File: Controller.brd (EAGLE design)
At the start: 100 x 66 mm, 20 parts, among them IC1 TB6612FNG

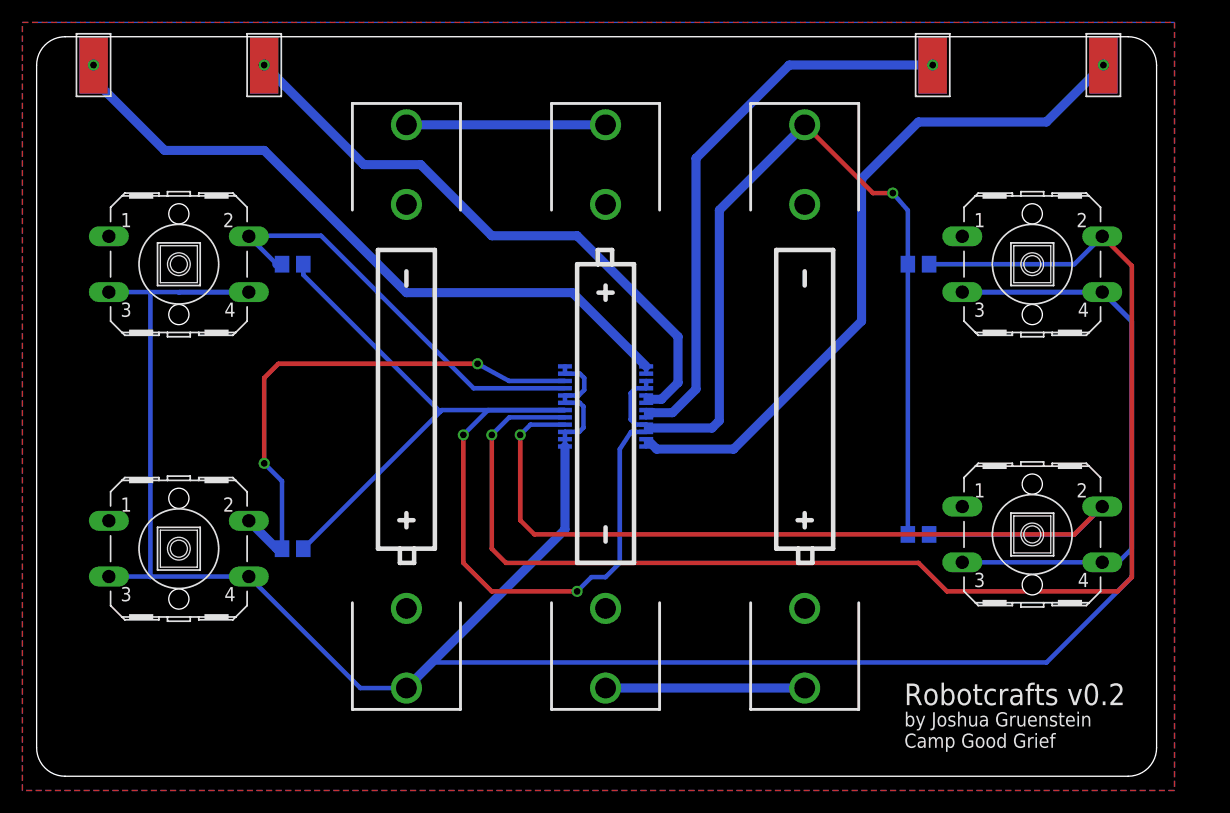
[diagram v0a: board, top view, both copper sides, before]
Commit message: cosmetic PCB upgrades
added OSHW logo to bottom silkscreen
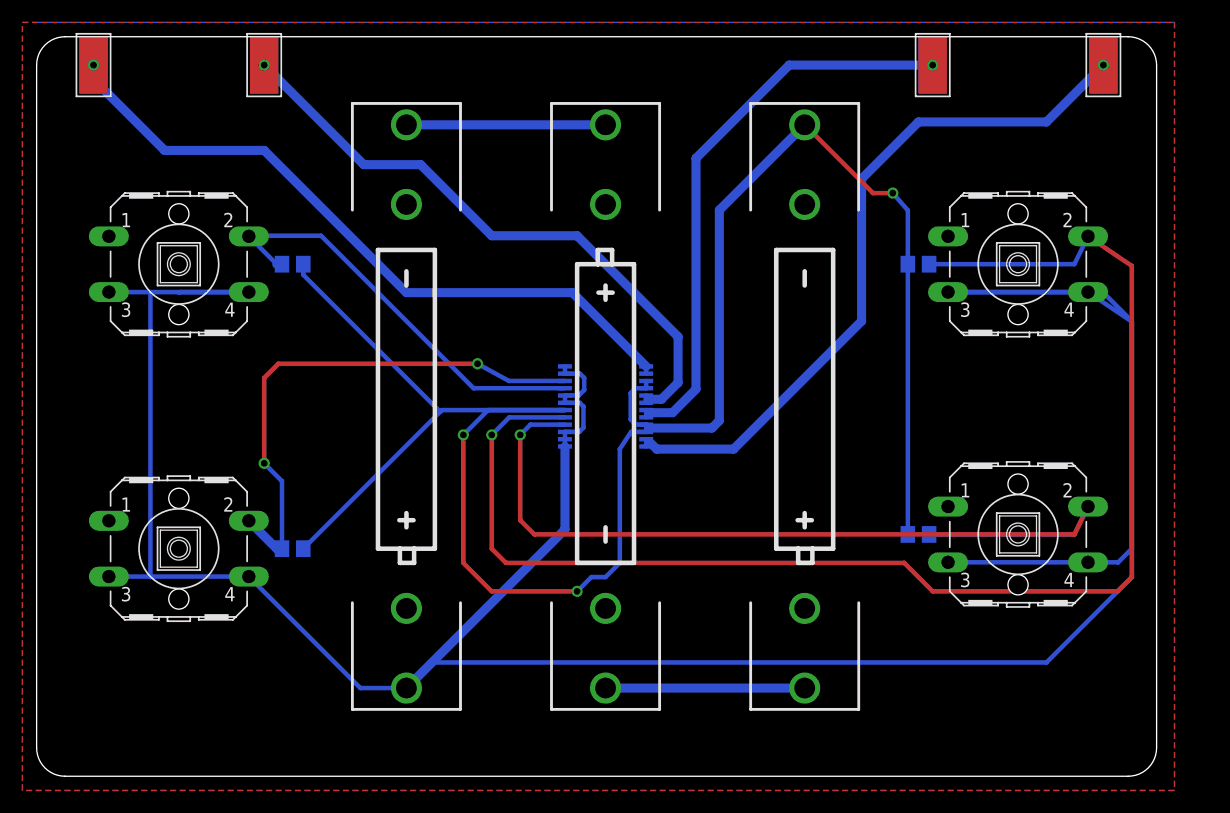
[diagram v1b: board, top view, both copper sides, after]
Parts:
- added GOLD_ORB_SM1: OSHWLOGO_GOLD_ORB_MED, bfl:OSHW1
- moved R_BCK_BTN 1.27 mm to (87.6, 21.6)
- moved R_FWD_BTN 1.27 mm to (87.6, 45.7)
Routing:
- net VCC: track 275.5 -> 279.0 mm
- net R_BCK: track 82.0 -> 80.5 mm
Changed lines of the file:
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@@
 <wire x1="97.46" y1="66.03" x2="2.54" y2="66.03" width="0" layer="20"/>
 <wire x1="2.54" y1="66.03" x2="0" y2="63.49" width="0" layer="20" curve="90"/>
-<text x="77.47" y="6.35" size="1.9304" layer="25">Robotcrafts v0.2</text>
-<text x="77.47" y="2.54" size="1.27" layer="25">by Joshua Gruenstein
+<text x="97.79" y="6.35" size="1.9304" layer="26" rot="MR0">Robotcrafts v0.2</text>
+<text x="97.79" y="2.54" size="1.27" layer="26" rot="MR0">by Joshua Gruenstein
 Camp Good Grief</text>
 </plain>
@@
 <element name="R3" library="rcl" package="R0805" value="10k" x="78.74" y="45.72" smashed="yes" rot="MR180"/>
 <element name="R4" library="rcl" package="R0805" value="10k" x="78.74" y="21.59" smashed="yes" rot="MR180"/>
-<element name="R_BCK_BTN" library="switch-omron" package="B3F-40XX" value="" x="88.9" y="21.59" smashed="yes">
-<attribute name="OC_NEWARK" value="36K3105" x="88.9" y="21.59" size="1.778" layer="27" display="off"/>
-<attribute name="MPN" value="B3F-4000" x="88.9" y="21.59" size="1.778" layer="27" display="off"/>
-<attribute name="MF" value="OMRON COMPONENTS USA" x="88.9" y="21.59" size="1.778" layer="27" display="off"/>
-<attribute name="OC_FARNELL" value="176434" x="88.9" y="21.59" size="1.778" layer="27" display="off"/>
-<attribute name="VALUE" x="85.725" y="16.51" size="1.27" layer="27" ratio="10"/>
-</element>
-<element name="R_FWD_BTN" library="switch-omron" package="B3F-40XX" value="" x="88.9" y="45.72" smashed="yes">
-<attribute name="OC_NEWARK" value="36K3105" x="88.9" y="45.72" size="1.778" layer="27" display="off"/>
-<attribute name="MPN" value="B3F-4000" x="88.9" y="45.72" size="1.778" layer="27" display="off"/>
-<attribute name="MF" value="OMRON COMPONENTS USA" x="88.9" y="45.72" size="1.778" layer="27" display="off"/>
-<attribute name="OC_FARNELL" value="176434" x="88.9" y="45.72" size="1.778" layer="27" display="off"/>
-<attribute name="VALUE" x="85.725" y="40.64" size="1.27" layer="27" ratio="10"/>
-</element>
+<element name="R_BCK_BTN" library="switch-omron" package="B3F-40XX" value="" x="87.63" y="21.59" smashed="yes">
+<attribute name="OC_NEWARK" value="36K3105" x="87.63" y="21.59" size="1.778" layer="27" display="off"/>
+<attribute name="MPN" value="B3F-4000" x="87.63" y="21.59" size="1.778" layer="27" display="off"/>
+<attribute name="MF" value="OMRON COMPONENTS USA" x="87.63" y="21.59" size="1.778" layer="27" display="off"/>
+<attribute name="OC_FARNELL" value="176434" x="87.63" y="21.59" size="1.778" layer="27" display="off"/>
+<attribute name="VALUE" x="84.455" y="16.51" size="1.27" layer="27" ratio="10"/>
+</element>
+<element name="R_FWD_BTN" library="switch-omron" package="B3F-40XX" value="" x="87.63" y="45.72" smashed="yes">
+<attribute name="OC_NEWARK" value="36K3105" x="87.63" y="45.72" size="1.778" layer="27" display="off"/>
+<attribute name="MPN" value="B3F-4000" x="87.63" y="45.72" size="1.778" layer="27" display="off"/>
+<attribute name="MF" value="OMRON COMPONENTS USA" x="87.63" y="45.72" size="1.778" layer="27" display="off"/>
+<attribute name="OC_FARNELL" value="176434" x="87.63" y="45.72" size="1.778" layer="27" display="off"/>
+<attribute name="VALUE" x="84.455" y="40.64" size="1.27" layer="27" ratio="10"/>
+</element>
+<element name="GOLD_ORB_SM1" library="bfl" package="OSHW1" value="OSHWLOGO_GOLD_ORB_MED" x="15.24" y="1.27" rot="MR0"/>
 </elements>
 <signals>
@@
 <wire x1="10.2108" y1="17.8308" x2="10.16" y2="17.78" width="0.4064" layer="16"/>
 <wire x1="10.16" y1="17.78" x2="10.16" y2="43.2308" width="0.4064" layer="16"/>
-<wire x1="82.6516" y1="43.2308" x2="95.1484" y2="43.2308" width="0.4064" layer="16"/>
-<wire x1="82.6516" y1="19.1008" x2="95.1484" y2="19.1008" width="0.4064" layer="16"/>
-<wire x1="95.1484" y1="19.1008" x2="96.5708" y2="19.1008" width="0.4064" layer="16"/>
+<wire x1="81.3816" y1="43.2308" x2="93.8784" y2="43.2308" width="0.4064" layer="16"/>
+<wire x1="81.3816" y1="19.1008" x2="93.8784" y2="19.1008" width="0.4064" layer="16"/>
+<wire x1="93.8784" y1="19.1008" x2="96.5708" y2="19.1008" width="0.4064" layer="16"/>
 <wire x1="96.5708" y1="19.1008" x2="97.79" y2="20.32" width="0.4064" layer="16"/>
 <wire x1="97.79" y1="20.32" x2="97.79" y2="40.5892" width="0.4064" layer="16"/>
-<wire x1="97.79" y1="40.5892" x2="95.1484" y2="43.2308" width="0.4064" layer="16"/>
-<wire x1="82.6516" y1="43.2308" x2="95.1992" y2="43.2308" width="0.4064" layer="16"/>
+<wire x1="97.79" y1="40.5892" x2="93.8784" y2="43.2308" width="0.4064" layer="16"/>
+<wire x1="81.3816" y1="43.2308" x2="95.1992" y2="43.2308" width="0.4064" layer="16"/>
 <wire x1="95.1992" y1="43.2308" x2="97.79" y2="40.64" width="0.4064" layer="16"/>
 <wire x1="97.79" y1="40.64" x2="97.79" y2="17.78" width="0.4064" layer="16"/>
@@
 <wire x1="40.64" y1="30.48" x2="40.64" y2="20.32" width="0.4064" layer="1"/>
 <wire x1="40.64" y1="20.32" x2="41.91" y2="19.05" width="0.4064" layer="1"/>
-<wire x1="41.91" y1="19.05" x2="78.74" y2="19.05" width="0.4064" layer="1"/>
-<wire x1="78.74" y1="19.05" x2="81.28" y2="16.51" width="0.4064" layer="1"/>
-<wire x1="81.28" y1="16.51" x2="96.52" y2="16.51" width="0.4064" layer="1"/>
+<wire x1="41.91" y1="19.05" x2="77.47" y2="19.05" width="0.4064" layer="1"/>
+<wire x1="77.47" y1="19.05" x2="80.01" y2="16.51" width="0.4064" layer="1"/>
+<wire x1="80.01" y1="16.51" x2="96.52" y2="16.51" width="0.4064" layer="1"/>
 <wire x1="96.52" y1="16.51" x2="97.79" y2="17.78" width="0.4064" layer="1"/>
 <wire x1="97.79" y1="17.78" x2="97.79" y2="45.5676" width="0.4064" layer="1"/>
-<wire x1="97.79" y1="45.5676" x2="95.1484" y2="48.2092" width="0.4064" layer="1"/>
-<wire x1="95.1484" y1="48.2092" x2="92.6592" y2="45.72" width="0.4064" layer="16"/>
+<wire x1="97.79" y1="45.5676" x2="93.8784" y2="48.2092" width="0.4064" layer="1"/>
+<wire x1="93.8784" y1="48.2092" x2="92.6592" y2="45.72" width="0.4064" layer="16"/>
 <wire x1="92.6592" y1="45.72" x2="79.69" y2="45.72" width="0.4064" layer="16"/>
 </signal>
@@
 <wire x1="43.18" y1="22.86" x2="44.45" y2="21.59" width="0.4064" layer="1"/>
 <wire x1="44.45" y1="21.59" x2="92.6592" y2="21.59" width="0.4064" layer="1"/>
-<wire x1="92.6592" y1="21.59" x2="95.1484" y2="24.0792" width="0.4064" layer="1"/>
+<wire x1="92.6592" y1="21.59" x2="93.8784" y2="24.0792" width="0.4064" layer="1"/>
 <wire x1="79.69" y1="21.59" x2="92.6592" y2="21.59" width="0.4064" layer="16"/>
-<wire x1="92.6592" y1="21.59" x2="95.1484" y2="24.0792" width="0.4064" layer="16"/>
+<wire x1="92.6592" y1="21.59" x2="93.8784" y2="24.0792" width="0.4064" layer="16"/>
 </signal>
 <signal name="L_OUT1">

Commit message: enlarge board alligator pad size
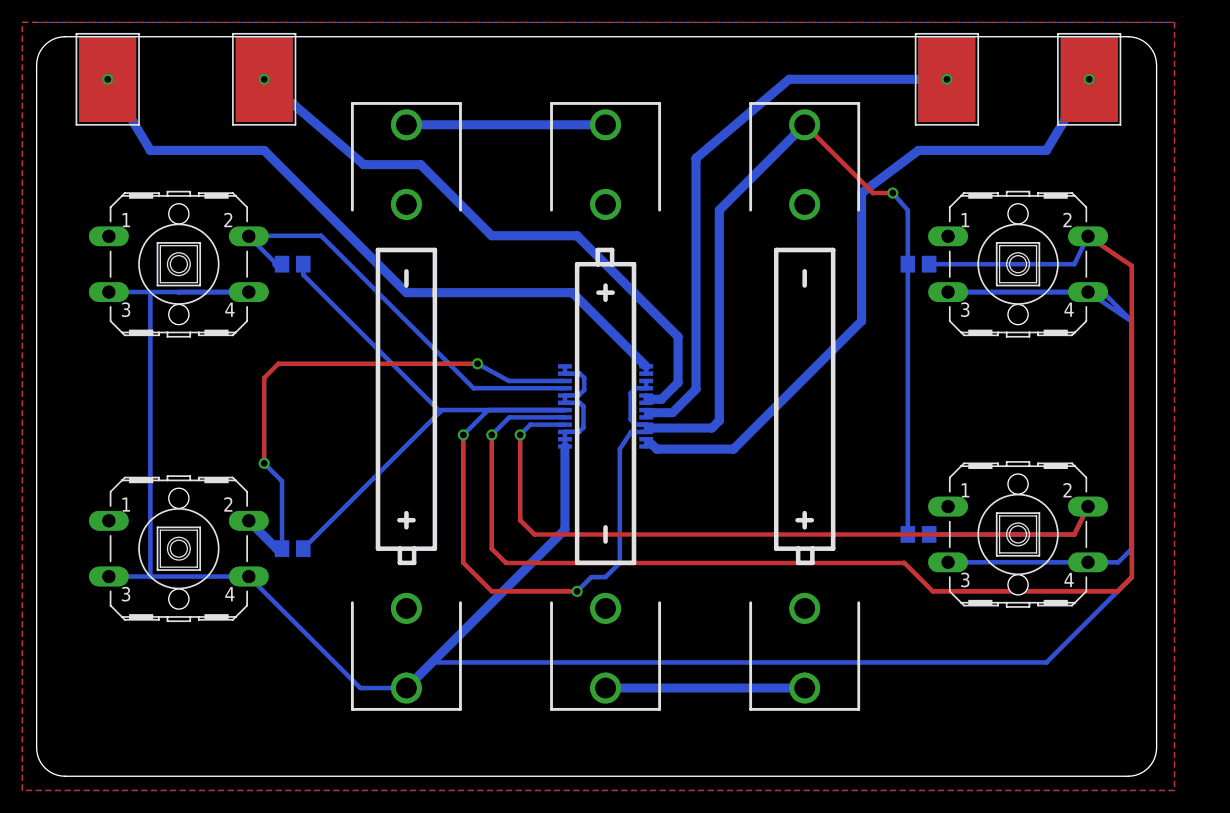
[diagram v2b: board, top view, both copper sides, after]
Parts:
- moved R1_PAD_FRONT 2.54 mm to (92.7, 63.5)
- moved L1_PAD_BACK 2.54 mm to (7.62, 63.5)
- moved R2_PAD_BACK 2.54 mm to (82.5, 63.5)
- moved L2_PAD_BACK 1.27 mm to (21.6, 63.5)
- moved L2_PAD_FRONT 1.27 mm to (19.1, 63.5)
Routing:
- net R_OUT1: track 63.5 -> 61.6 mm
- net L_OUT1: track 61.9 -> 60.3 mm
- net L_OUT2: track 55.5 -> 54.6 mm
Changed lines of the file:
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@@
 </element>
 <element name="IC1" library="adafruit" package="SSOP24" value="TB6612FNG" x="50.8" y="33.02" smashed="yes" rot="MR270"/>
-<element name="L1_PAD_BACK" library="wirepad" package="5-2,5" value="WIREPADSMD5-2,5" x="5.08" y="63.5" smashed="yes" rot="MR0">
-<attribute name="VALUE" x="5.18" y="66.3" size="0.0254" layer="28" rot="MR0"/>
+<element name="L1_PAD_BACK" library="wirepad" package="5-2,5" value="WIREPADSMD5-2,5" x="7.62" y="63.5" smashed="yes" rot="MR0">
+<attribute name="VALUE" x="7.72" y="66.3" size="0.0254" layer="28" rot="MR0"/>
 </element>
 <element name="L1_PAD_FRONT" library="wirepad" package="5-2,5" value="WIREPADSMD5-2,5" x="5.08" y="63.5" smashed="yes">
 <attribute name="VALUE" x="4.98" y="66.3" size="0.0254" layer="27"/>
 </element>
-<element name="L2_PAD_BACK" library="wirepad" package="5-2,5" value="WIREPADSMD5-2,5" x="20.32" y="63.5" smashed="yes" rot="MR0">
-<attribute name="VALUE" x="20.42" y="66.3" size="0.0254" layer="28" rot="MR0"/>
-</element>
-<element name="L2_PAD_FRONT" library="wirepad" package="5-2,5" value="WIREPADSMD5-2,5" x="20.32" y="63.5" smashed="yes">
-<attribute name="VALUE" x="20.22" y="66.3" size="0.0254" layer="27"/>
+<element name="L2_PAD_BACK" library="wirepad" package="5-2,5" value="WIREPADSMD5-2,5" x="21.59" y="63.5" smashed="yes" rot="MR0">
+<attribute name="VALUE" x="21.69" y="66.3" size="0.0254" layer="28" rot="MR0"/>
+</element>
+<element name="L2_PAD_FRONT" library="wirepad" package="5-2,5" value="WIREPADSMD5-2,5" x="19.05" y="63.5" smashed="yes">
+<attribute name="VALUE" x="18.95" y="66.3" size="0.0254" layer="27"/>
 </element>
 <element name="L_BCK_BTN" library="switch-omron" package="B3F-40XX" value="" x="12.7" y="20.32" smashed="yes">
@@
 <attribute name="VALUE" x="95.35" y="66.3" size="0.0254" layer="28" rot="MR0"/>
 </element>
-<element name="R1_PAD_FRONT" library="wirepad" package="5-2,5" value="WIREPADSMD5-2,5" x="95.25" y="63.5" smashed="yes">
-<attribute name="VALUE" x="95.15" y="66.3" size="0.0254" layer="27"/>
+<element name="R1_PAD_FRONT" library="wirepad" package="5-2,5" value="WIREPADSMD5-2,5" x="92.71" y="63.5" smashed="yes">
+<attribute name="VALUE" x="92.61" y="66.3" size="0.0254" layer="27"/>
 </element>
 <element name="R2" library="rcl" package="R0805" value="10k" x="22.86" y="20.32" smashed="yes" rot="MR0"/>
-<element name="R2_PAD_BACK" library="wirepad" package="5-2,5" value="WIREPADSMD5-2,5" x="80.01" y="63.5" smashed="yes" rot="MR0">
-<attribute name="VALUE" x="80.11" y="66.3" size="0.0254" layer="28" rot="MR0"/>
+<element name="R2_PAD_BACK" library="wirepad" package="5-2,5" value="WIREPADSMD5-2,5" x="82.55" y="63.5" smashed="yes" rot="MR0">
+<attribute name="VALUE" x="82.65" y="66.3" size="0.0254" layer="28" rot="MR0"/>
 </element>
 <element name="R2_PAD_FRONT" library="wirepad" package="5-2,5" value="WIREPADSMD5-2,5" x="80.01" y="63.5" smashed="yes">
@@
 <contactref element="IC1" pad="1"/>
 <contactref element="IC1" pad="2"/>
-<contactref element="L1_PAD_BACK" pad="1"/>
 <contactref element="L1_PAD_FRONT" pad="1"/>
 <wire x1="54.425" y1="35.945" x2="54.425" y2="36.595" width="0.4064" layer="16"/>
-<via x="5.08" y="63.5" extent="1-16" drill="0.6" shape="square"/>
 <wire x1="54.425" y1="36.595" x2="47.84" y2="43.18" width="0.8128" layer="16"/>
 <wire x1="47.84" y1="43.18" x2="33.02" y2="43.18" width="0.8128" layer="16"/>
 <wire x1="33.02" y1="43.18" x2="20.32" y2="55.88" width="0.8128" layer="16"/>
-<wire x1="20.32" y1="55.88" x2="11.43" y2="55.88" width="0.8128" layer="16"/>
-<wire x1="11.43" y1="55.88" x2="5.08" y2="62.23" width="0.8128" layer="16"/>
-<wire x1="5.08" y1="62.23" x2="5.08" y2="63.5" width="0.8128" layer="16"/>
+<wire x1="20.32" y1="55.88" x2="10.16" y2="55.88" width="0.8128" layer="16"/>
+<contactref element="L1_PAD_BACK" pad="1"/>
+<wire x1="10.16" y1="55.88" x2="6.35" y2="62.23" width="0.8128" layer="16"/>
+<via x="6.35" y="62.23" extent="1-16" drill="0.6" shape="square"/>
 </signal>
 <signal name="L_OUT2">
 <contactref element="IC1" pad="5"/>
 <contactref element="IC1" pad="6"/>
-<contactref element="L2_PAD_BACK" pad="1"/>
 <contactref element="L2_PAD_FRONT" pad="1"/>
 <wire x1="54.425" y1="33.995" x2="54.425" y2="33.345" width="0.4064" layer="16"/>
-<via x="20.32" y="63.5" extent="1-16" drill="0.6" shape="square"/>
+<via x="20.32" y="62.23" extent="1-16" drill="0.6" shape="square"/>
 <wire x1="54.425" y1="33.995" x2="54.425" y2="33.8072625" width="0.4064" layer="16"/>
 <wire x1="54.425" y1="33.8072625" x2="54.573165625" y2="33.659096875" width="0.4064" layer="16"/>
@@
 <wire x1="40.64" y1="48.26" x2="34.29" y2="54.61" width="0.8128" layer="16"/>
 <wire x1="34.29" y1="54.61" x2="29.21" y2="54.61" width="0.8128" layer="16"/>
-<wire x1="29.21" y1="54.61" x2="20.32" y2="63.5" width="0.8128" layer="16"/>
+<wire x1="29.21" y1="54.61" x2="20.32" y2="62.23" width="0.8128" layer="16"/>
+<contactref element="L2_PAD_BACK" pad="1"/>
 </signal>
 <signal name="R_OUT2">
@@
 <contactref element="R2_PAD_FRONT" pad="1"/>
 <wire x1="54.425" y1="32.695" x2="54.425" y2="32.045" width="0.4064" layer="16"/>
-<via x="80.01" y="63.5" extent="1-16" drill="0.6" shape="square"/>
+<via x="81.28" y="62.23" extent="1-16" drill="0.6" shape="square"/>
 <wire x1="54.425" y1="32.695" x2="54.7348" y2="32.3852" width="0.4064" layer="16"/>
 <wire x1="54.7348" y1="32.3852" x2="54.863325" y2="32.3852" width="0.4064" layer="16"/>
@@
 <wire x1="56.77639375" y1="32.46074375" x2="58.875134375" y2="34.559484375" width="0.8128" layer="16"/>
 <wire x1="58.875134375" y1="34.559484375" x2="58.875134375" y2="55.176959375" width="0.8128" layer="16"/>
-<wire x1="58.875134375" y1="55.176959375" x2="67.198175" y2="63.5" width="0.8128" layer="16"/>
-<wire x1="67.198175" y1="63.5" x2="80.01" y2="63.5" width="0.8128" layer="16"/>
+<wire x1="58.875134375" y1="55.176959375" x2="67.198175" y2="62.23" width="0.8128" layer="16"/>
+<wire x1="67.198175" y1="62.23" x2="81.28" y2="62.23" width="0.8128" layer="16"/>
 </signal>
 <signal name="R_OUT1">
@@
 <contactref element="R1_PAD_FRONT" pad="1"/>
 <wire x1="54.425" y1="29.445" x2="54.425" y2="30.095" width="0.4064" layer="16"/>
-<via x="95.25" y="63.5" extent="1-16" drill="0.6" shape="square"/>
+<via x="93.98" y="62.23" extent="1-16" drill="0.6" shape="square"/>
 <wire x1="54.425" y1="30.095" x2="54.76035625" y2="29.75964375" width="0.4064" layer="16"/>
 <wire x1="54.76035625" y1="29.75964375" x2="54.81419375" y2="29.75964375" width="0.4064" layer="16"/>
@@
 <wire x1="55.3638375" y1="29.21" x2="62.23" y2="29.21" width="0.8128" layer="16"/>
 <wire x1="62.23" y1="29.21" x2="73.66" y2="40.64" width="0.8128" layer="16"/>
-<wire x1="73.66" y1="40.64" x2="73.66" y2="53.34" width="0.8128" layer="16"/>
-<wire x1="73.66" y1="53.34" x2="78.74" y2="58.42" width="0.8128" layer="16"/>
-<wire x1="78.74" y1="58.42" x2="90.17" y2="58.42" width="0.8128" layer="16"/>
-<wire x1="90.17" y1="58.42" x2="95.25" y2="63.5" width="0.8128" layer="16"/>
+<wire x1="73.66" y1="40.64" x2="73.66" y2="52.07" width="0.8128" layer="16"/>
+<wire x1="73.66" y1="52.07" x2="78.74" y2="55.88" width="0.8128" layer="16"/>
+<wire x1="78.74" y1="55.88" x2="90.17" y2="55.88" width="0.8128" layer="16"/>
+<wire x1="90.17" y1="55.88" x2="93.98" y2="62.23" width="0.8128" layer="16"/>
 </signal>
 </signals>
